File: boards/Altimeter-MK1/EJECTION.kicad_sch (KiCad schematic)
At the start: 38 parts, among them Q1 AOD442G

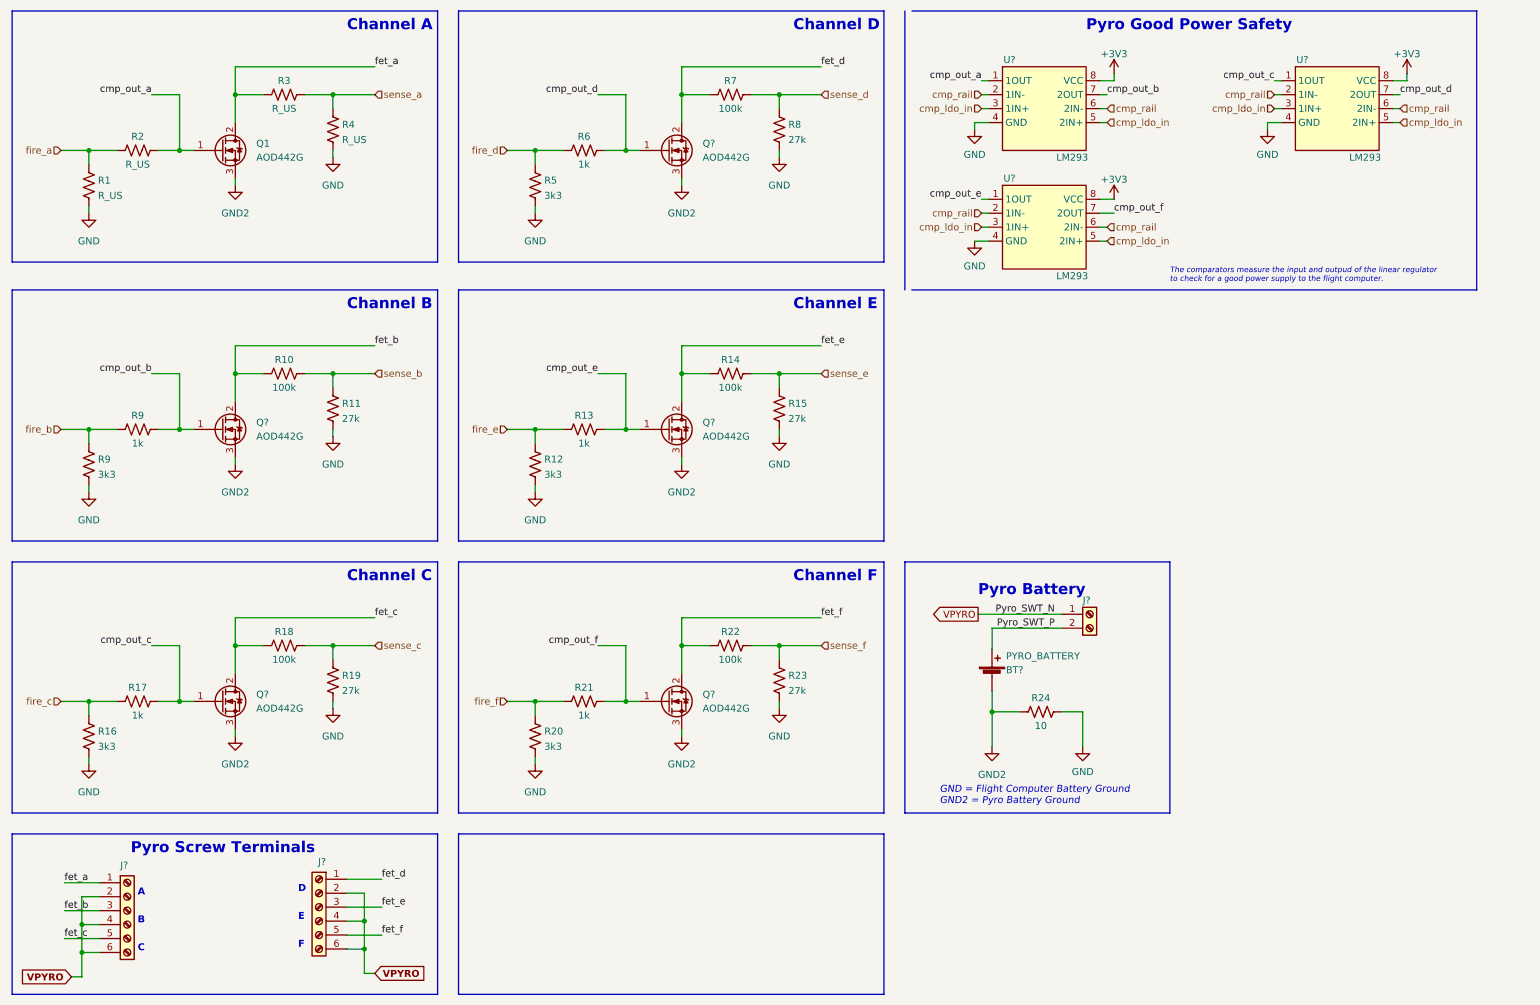
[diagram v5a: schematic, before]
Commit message: REBBASE BRANCHES - Worked on b2b connections
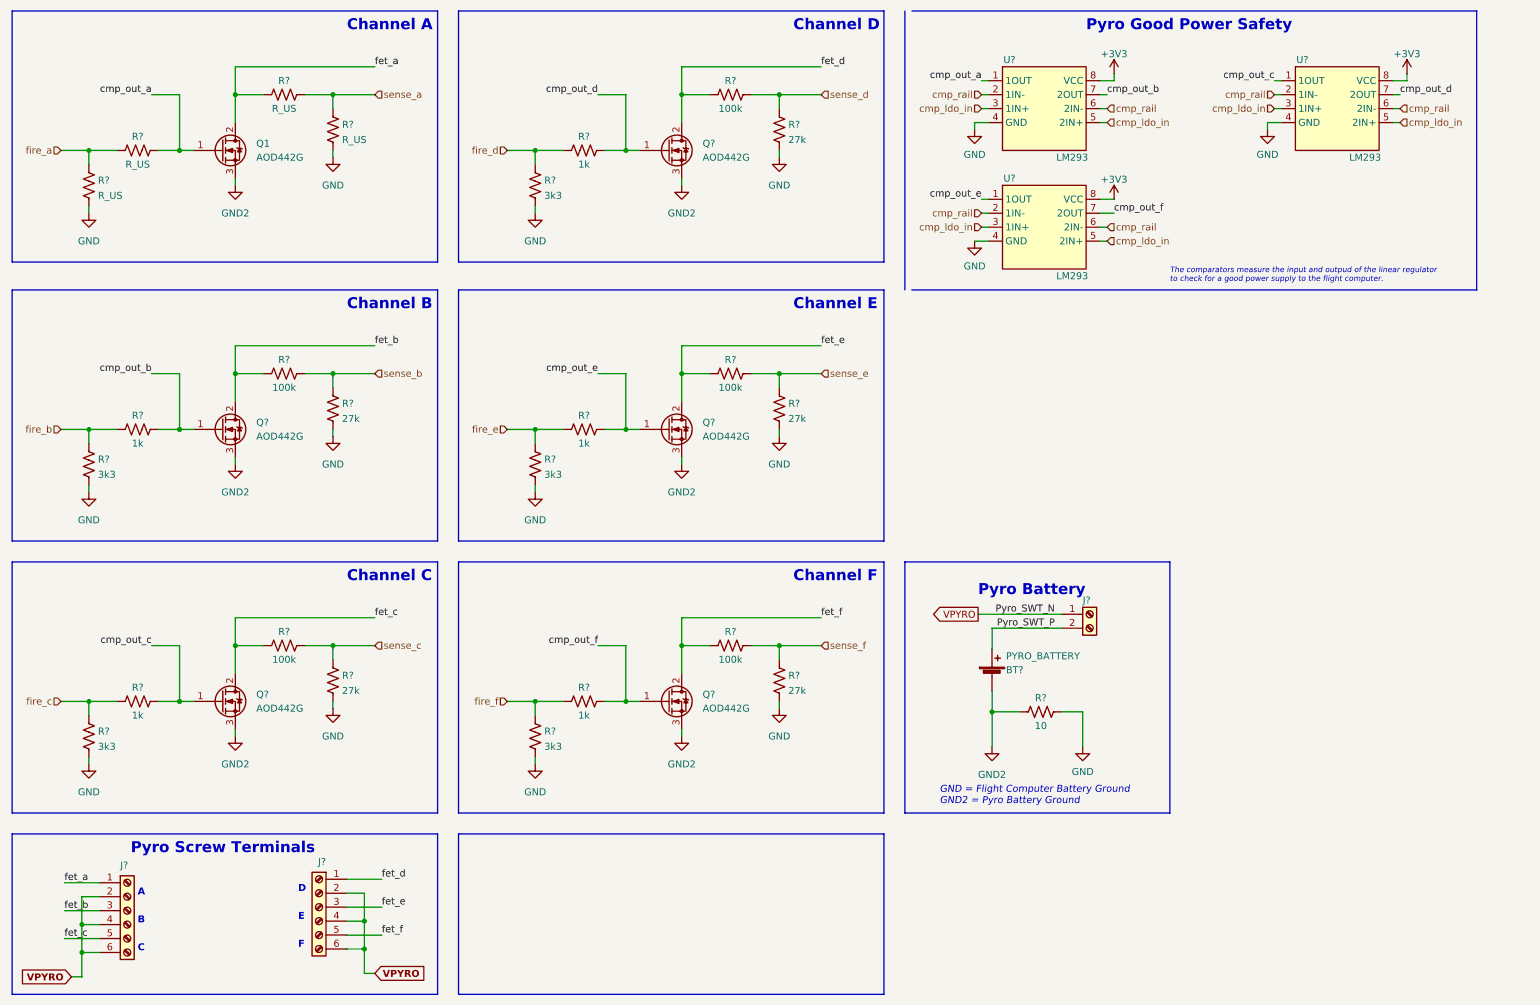
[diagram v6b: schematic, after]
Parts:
- renumbered R20 to R?, R3 to R?, R9 to R?, R19 to R?, R4 to R?, R18 to R?, R22 to R?, R21 to R?, R5 to R?, R1 to R?, R7 to R?, R8 to R?, R17 to R?, R16 to R?, R23 to R?, R14 to R?, R13 to R?, R12 to R?, R6 to R?, R15 to R?, R2 to R?, R11 to R?, R10 to R?, R24 to R?
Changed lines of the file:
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@@
   (symbol (lib_id "Device:R_US") (at 110.49 147.32 0) (unit 1)
     (in_bom yes) (on_board yes) (fields_autoplaced)
-    (property "Reference" "R20" (id 0) (at 112.141 146.4115 0)
+    (property "Reference" "R?" (id 0) (at 112.141 146.4115 0)
       (effects (font (size 1.27 1.27)) (justify left))
     )
@@
   (symbol (lib_id "Device:R_US") (at 64.77 30.48 90) (unit 1)
     (in_bom yes) (on_board yes)
-    (property "Reference" "R3" (id 0) (at 64.77 27.94 90))
+    (property "Reference" "R?" (id 0) (at 64.77 27.94 90))
     (property "Value" "R_US" (id 1) (at 64.77 33.02 90))
     (property "Footprint" "Resistor_SMD:R_01005_0402Metric" (id 2) (at 65.024 29.464 90)
@@
   (symbol (lib_id "Device:R_US") (at 38.1 91.44 90) (unit 1)
     (in_bom yes) (on_board yes)
-    (property "Reference" "R9" (id 0) (at 38.1 88.9 90))
+    (property "Reference" "R?" (id 0) (at 38.1 88.9 90))
     (property "Value" "1k" (id 1) (at 38.1 93.98 90))
     (property "Footprint" "Resistor_SMD:R_01005_0402Metric" (id 2) (at 38.354 90.424 90)
@@
   (symbol (lib_id "Device:R_US") (at 73.66 137.16 0) (unit 1)
     (in_bom yes) (on_board yes) (fields_autoplaced)
-    (property "Reference" "R19" (id 0) (at 75.311 136.2515 0)
+    (property "Reference" "R?" (id 0) (at 75.311 136.2515 0)
       (effects (font (size 1.27 1.27)) (justify left))
     )
@@
   (symbol (lib_id "Device:R_US") (at 73.66 36.83 0) (unit 1)
     (in_bom yes) (on_board yes) (fields_autoplaced)
-    (property "Reference" "R4" (id 0) (at 75.311 35.9215 0)
+    (property "Reference" "R?" (id 0) (at 75.311 35.9215 0)
       (effects (font (size 1.27 1.27)) (justify left))
     )
@@
   (symbol (lib_id "Device:R_US") (at 64.77 130.81 90) (unit 1)
     (in_bom yes) (on_board yes)
-    (property "Reference" "R18" (id 0) (at 64.77 128.27 90))
+    (property "Reference" "R?" (id 0) (at 64.77 128.27 90))
     (property "Value" "100k" (id 1) (at 64.77 133.35 90))
     (property "Footprint" "Resistor_SMD:R_01005_0402Metric" (id 2) (at 65.024 129.794 90)
@@
   (symbol (lib_id "Device:R_US") (at 146.05 130.81 90) (unit 1)
     (in_bom yes) (on_board yes)
-    (property "Reference" "R22" (id 0) (at 146.05 128.27 90))
+    (property "Reference" "R?" (id 0) (at 146.05 128.27 90))
     (property "Value" "100k" (id 1) (at 146.05 133.35 90))
     (property "Footprint" "Resistor_SMD:R_01005_0402Metric" (id 2) (at 146.304 129.794 90)
@@
   (symbol (lib_id "Device:R_US") (at 119.38 140.97 90) (unit 1)
     (in_bom yes) (on_board yes)
-    (property "Reference" "R21" (id 0) (at 119.38 138.43 90))
+    (property "Reference" "R?" (id 0) (at 119.38 138.43 90))
     (property "Value" "1k" (id 1) (at 119.38 143.51 90))
     (property "Footprint" "Resistor_SMD:R_01005_0402Metric" (id 2) (at 119.634 139.954 90)
@@
   (symbol (lib_id "Device:R_US") (at 110.49 46.99 0) (unit 1)
     (in_bom yes) (on_board yes) (fields_autoplaced)
-    (property "Reference" "R5" (id 0) (at 112.141 46.0815 0)
+    (property "Reference" "R?" (id 0) (at 112.141 46.0815 0)
       (effects (font (size 1.27 1.27)) (justify left))
     )
@@
   (symbol (lib_id "Device:R_US") (at 29.21 46.99 0) (unit 1)
     (in_bom yes) (on_board yes) (fields_autoplaced)
-    (property "Reference" "R1" (id 0) (at 30.861 46.0815 0)
+    (property "Reference" "R?" (id 0) (at 30.861 46.0815 0)
       (effects (font (size 1.27 1.27)) (justify left))
     )
@@
   (symbol (lib_id "Device:R_US") (at 146.05 30.48 90) (unit 1)
     (in_bom yes) (on_board yes)
-    (property "Reference" "R7" (id 0) (at 146.05 27.94 90))
+    (property "Reference" "R?" (id 0) (at 146.05 27.94 90))
     (property "Value" "100k" (id 1) (at 146.05 33.02 90))
     (property "Footprint" "Resistor_SMD:R_01005_0402Metric" (id 2) (at 146.304 29.464 90)
@@
   (symbol (lib_id "Device:R_US") (at 154.94 36.83 0) (unit 1)
     (in_bom yes) (on_board yes) (fields_autoplaced)
-    (property "Reference" "R8" (id 0) (at 156.591 35.9215 0)
+    (property "Reference" "R?" (id 0) (at 156.591 35.9215 0)
       (effects (font (size 1.27 1.27)) (justify left))
     )
@@
   (symbol (lib_id "Device:R_US") (at 38.1 140.97 90) (unit 1)
     (in_bom yes) (on_board yes)
-    (property "Reference" "R17" (id 0) (at 38.1 138.43 90))
+    (property "Reference" "R?" (id 0) (at 38.1 138.43 90))
     (property "Value" "1k" (id 1) (at 38.1 143.51 90))
     (property "Footprint" "Resistor_SMD:R_01005_0402Metric" (id 2) (at 38.354 139.954 90)
@@
   (symbol (lib_id "Device:R_US") (at 29.21 147.32 0) (unit 1)
     (in_bom yes) (on_board yes) (fields_autoplaced)
-    (property "Reference" "R16" (id 0) (at 30.861 146.4115 0)
+    (property "Reference" "R?" (id 0) (at 30.861 146.4115 0)
       (effects (font (size 1.27 1.27)) (justify left))
     )
@@
   (symbol (lib_id "Device:R_US") (at 154.94 137.16 0) (unit 1)
     (in_bom yes) (on_board yes) (fields_autoplaced)
-    (property "Reference" "R23" (id 0) (at 156.591 136.2515 0)
+    (property "Reference" "R?" (id 0) (at 156.591 136.2515 0)
       (effects (font (size 1.27 1.27)) (justify left))
     )
@@
   (symbol (lib_id "Device:R_US") (at 146.05 81.28 90) (unit 1)
     (in_bom yes) (on_board yes)
-    (property "Reference" "R14" (id 0) (at 146.05 78.74 90))
+    (property "Reference" "R?" (id 0) (at 146.05 78.74 90))
     (property "Value" "100k" (id 1) (at 146.05 83.82 90))
     (property "Footprint" "Resistor_SMD:R_01005_0402Metric" (id 2) (at 146.304 80.264 90)
@@
   (symbol (lib_id "Device:R_US") (at 119.38 91.44 90) (unit 1)
     (in_bom yes) (on_board yes)
-    (property "Reference" "R13" (id 0) (at 119.38 88.9 90))
+    (property "Reference" "R?" (id 0) (at 119.38 88.9 90))
     (property "Value" "1k" (id 1) (at 119.38 93.98 90))
     (property "Footprint" "Resistor_SMD:R_01005_0402Metric" (id 2) (at 119.634 90.424 90)
@@
   (symbol (lib_id "Device:R_US") (at 110.49 97.79 0) (unit 1)
     (in_bom yes) (on_board yes) (fields_autoplaced)
-    (property "Reference" "R12" (id 0) (at 112.141 96.8815 0)
+    (property "Reference" "R?" (id 0) (at 112.141 96.8815 0)
       (effects (font (size 1.27 1.27)) (justify left))
     )
@@
   (symbol (lib_id "Device:R_US") (at 119.38 40.64 90) (unit 1)
     (in_bom yes) (on_board yes)
-    (property "Reference" "R6" (id 0) (at 119.38 38.1 90))
+    (property "Reference" "R?" (id 0) (at 119.38 38.1 90))
     (property "Value" "1k" (id 1) (at 119.38 43.18 90))
     (property "Footprint" "Resistor_SMD:R_01005_0402Metric" (id 2) (at 119.634 39.624 90)
@@
   (symbol (lib_id "Device:R_US") (at 29.21 97.79 0) (unit 1)
     (in_bom yes) (on_board yes) (fields_autoplaced)
-    (property "Reference" "R9" (id 0) (at 30.861 96.8815 0)
+    (property "Reference" "R?" (id 0) (at 30.861 96.8815 0)
       (effects (font (size 1.27 1.27)) (justify left))
     )
@@
   (symbol (lib_id "Device:R_US") (at 154.94 87.63 0) (unit 1)
     (in_bom yes) (on_board yes) (fields_autoplaced)
-    (property "Reference" "R15" (id 0) (at 156.591 86.7215 0)
+    (property "Reference" "R?" (id 0) (at 156.591 86.7215 0)
       (effects (font (size 1.27 1.27)) (justify left))
     )
@@
   (symbol (lib_id "Device:R_US") (at 38.1 40.64 90) (unit 1)
     (in_bom yes) (on_board yes)
-    (property "Reference" "R2" (id 0) (at 38.1 38.1 90))
+    (property "Reference" "R?" (id 0) (at 38.1 38.1 90))
     (property "Value" "R_US" (id 1) (at 38.1 43.18 90))
     (property "Footprint" "Resistor_SMD:R_01005_0402Metric" (id 2) (at 38.354 39.624 90)
@@
   (symbol (lib_id "Device:R_US") (at 73.66 87.63 0) (unit 1)
     (in_bom yes) (on_board yes) (fields_autoplaced)
-    (property "Reference" "R11" (id 0) (at 75.311 86.7215 0)
+    (property "Reference" "R?" (id 0) (at 75.311 86.7215 0)
       (effects (font (size 1.27 1.27)) (justify left))
     )
@@
   (symbol (lib_id "Device:R_US") (at 64.77 81.28 90) (unit 1)
     (in_bom yes) (on_board yes)
-    (property "Reference" "R10" (id 0) (at 64.77 78.74 90))
+    (property "Reference" "R?" (id 0) (at 64.77 78.74 90))
     (property "Value" "100k" (id 1) (at 64.77 83.82 90))
     (property "Footprint" "Resistor_SMD:R_01005_0402Metric" (id 2) (at 65.024 80.264 90)
@@
   (symbol (lib_id "Device:R_US") (at 202.565 142.875 90) (unit 1)
     (in_bom yes) (on_board yes)
-    (property "Reference" "R24" (id 0) (at 202.565 140.335 90))
+    (property "Reference" "R?" (id 0) (at 202.565 140.335 90))
     (property "Value" "10" (id 1) (at 202.565 145.415 90))
     (property "Footprint" "Resistor_SMD:R_01005_0402Metric" (id 2) (at 202.819 141.859 90)

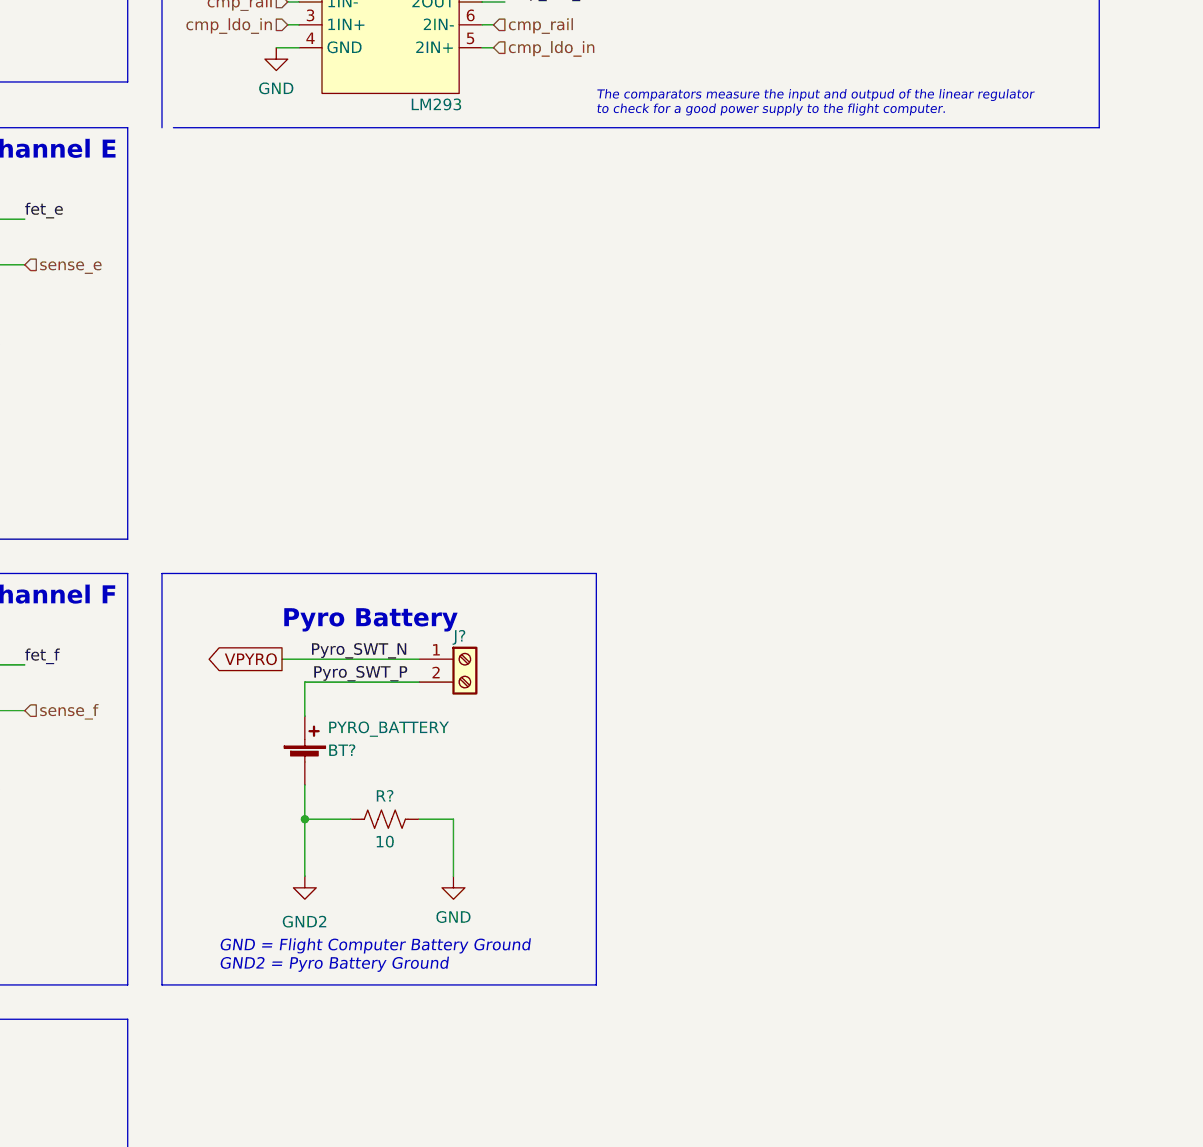
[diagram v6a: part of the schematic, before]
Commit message: Redefined labels
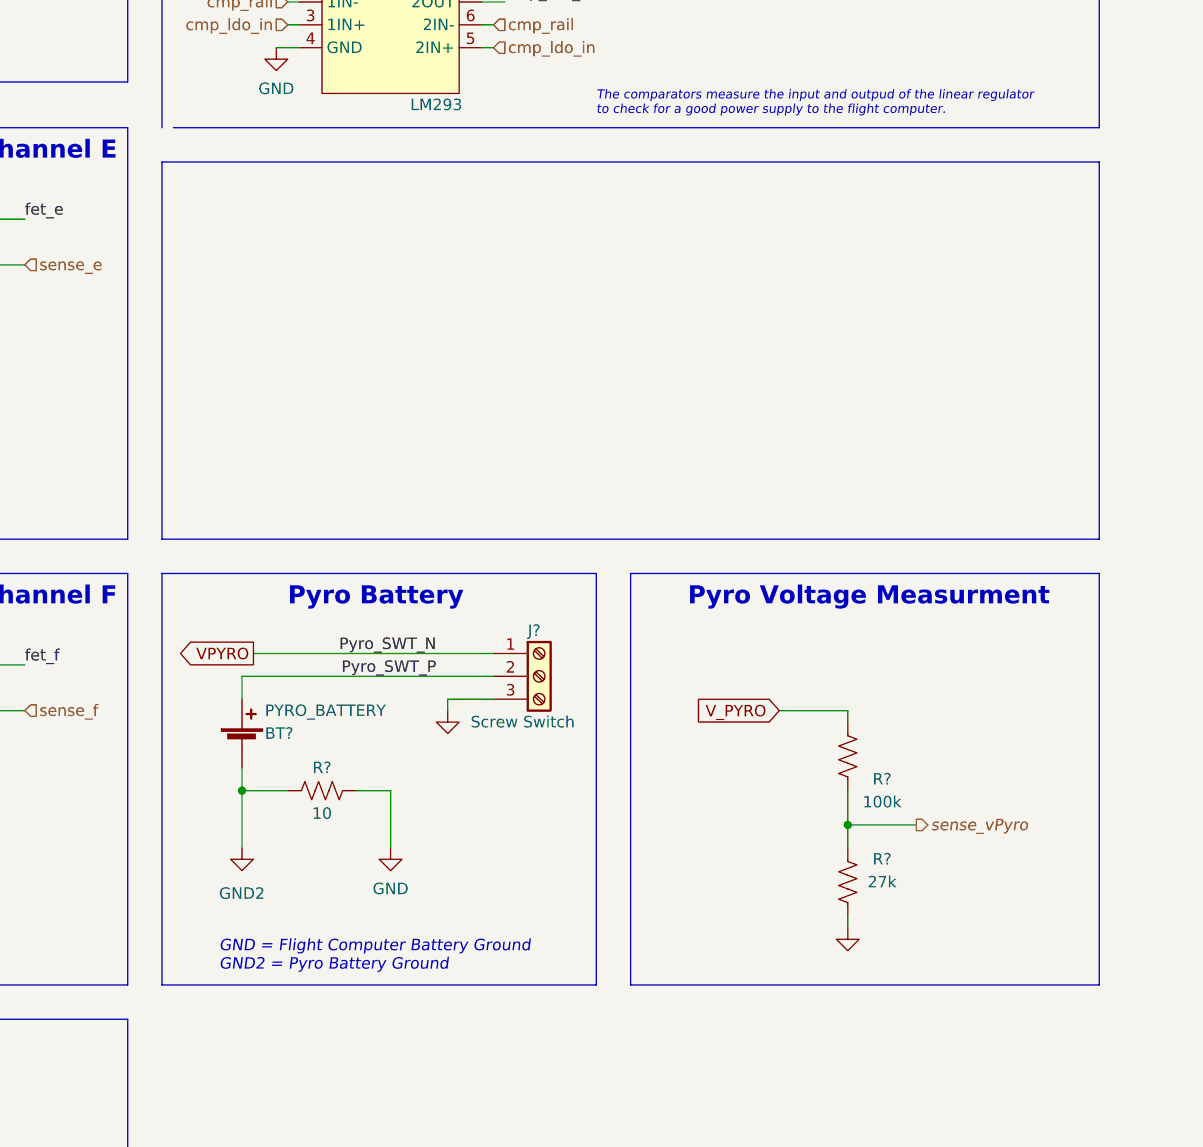
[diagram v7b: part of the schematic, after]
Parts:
- removed J?: ~, symbol Connector:Screw_Terminal_01x02
- added J?: Screw Switch, symbol Connector:Screw_Terminal_01x03
- added R?: 100k, symbol Device:R_US
- added R?: 27k, symbol Device:R_US
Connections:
- net GND: now also J?.3 (Pin_3), R?.2
- net Pyro_SWT_P: now also J?.2 (Pin_2)
- net VPYRO: now also J?.1 (Pin_1)
- new net V_PYRO: R?.2
- new net sense_vPyro: R?.1, R?.1
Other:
- note added: "Pyro Voltage Measurment"
- moved on the sheet: BT?, R?
